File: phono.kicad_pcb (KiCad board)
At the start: 2 copper layers, 98.5 x 82 mm, 63 parts, among them J1 Power +30V, J2 R Phono in, J3 L Phono in, J4 R Phono out, J5 L Phono out, Q1 2N2222, Q2 2N2222, Q3 2N2222, Q4 2N2222, Q5 2N2222, Q6 2N2222

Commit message: Add files via upload
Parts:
- removed C10: 47uf, Capacitor_THT:CP_Radial_D6.3mm_P2.50mm
- removed C11, C12, C13, C14, C15, C16, C17: 150uf, Capacitor_THT:CP_Radial_D10.0mm_P5.00mm
- removed C18: 15uf, Capacitor_THT:CP_Radial_D5.0mm_P2.00mm
- removed C19, C21: 6.8nf, Capacitor_THT:C_Rect_L7.0mm_W2.0mm_P5.00mm
- removed C20, C22: 22nf, Capacitor_THT:C_Rect_L7.0mm_W2.0mm_P5.00mm
- removed D1, D2: 1N5250B, Diode_THT:D_DO-41_SOD81_P10.16mm_Horizontal
- removed J4: R Phono out, Connector_Wire:SolderWire-2sqmm_1x01_D2mm_OD3.9mm
- removed J5: L Phono out, Connector_Wire:SolderWire-2sqmm_1x01_D2mm_OD3.9mm
- removed Q4, Q5, Q6: 2N2222, Package_TO_SOT_THT:TO-18-3
- removed R16: 47k, Resistor_THT:R_Axial_DIN0207_L6.3mm_D2.5mm_P10.16mm_Horizontal
- removed R17: 8k2, Resistor_THT:R_Axial_DIN0207_L6.3mm_D2.5mm_P10.16mm_Horizontal
- removed R18: 150, Resistor_THT:R_Axial_DIN0207_L6.3mm_D2.5mm_P10.16mm_Horizontal
- removed R19, R26: 1k8, Resistor_THT:R_Axial_DIN0207_L6.3mm_D2.5mm_P10.16mm_Horizontal
- removed R20: 1k, Resistor_THT:R_Axial_DIN0207_L6.3mm_D2.5mm_P10.16mm_Horizontal
- removed R21: 12k, Resistor_THT:R_Axial_DIN0207_L6.3mm_D2.5mm_P10.16mm_Horizontal
- removed R22: 270k, Resistor_THT:R_Axial_DIN0207_L6.3mm_D2.5mm_P10.16mm_Horizontal
- removed R23: 680, Resistor_THT:R_Axial_DIN0207_L6.3mm_D2.5mm_P10.16mm_Horizontal
- removed R24: 6k, Resistor_THT:R_Axial_DIN0207_L6.3mm_D2.5mm_P10.16mm_Horizontal
- removed R25: 100, Resistor_THT:R_Axial_DIN0207_L6.3mm_D2.5mm_P10.16mm_Horizontal
- removed R27: 4k7, Resistor_THT:R_Axial_DIN0207_L6.3mm_D2.5mm_P10.16mm_Horizontal
- removed R28: 10k, Resistor_THT:R_Axial_DIN0207_L6.3mm_D2.5mm_P10.16mm_Horizontal
- added C101: 300u, Capacitor_THT:CP_Radial_D10.0mm_P5.00mm, F.Cu at (86.2, 96.3)
- added C102: 300u, Capacitor_THT:CP_Radial_D10.0mm_P5.00mm, F.Cu at (77.1, 85.1)
- added C103: 6n8, Capacitor_THT:C_Axial_L3.8mm_D2.6mm_P10.00mm_Horizontal, F.Cu at (96.3, 79.7)
- added C104: 22n, Capacitor_THT:C_Axial_L3.8mm_D2.6mm_P10.00mm_Horizontal, F.Cu at (103.9, 79.7)
- added C105: 47u, Capacitor_THT:CP_Radial_D10.0mm_P5.00mm, F.Cu at (121.0, 96.3)
- added C106: 1uF, Capacitor_THT:C_Axial_L3.8mm_D2.6mm_P10.00mm_Horizontal, F.Cu at (73.4, 69.8)
- added Down-Left1: MountingHole_3.2mm_M3, MountingHole:MountingHole_3.2mm_M3, F.Cu at (62.9, 109.9)
- added Down-Right1: MountingHole_3.2mm_M3, MountingHole:MountingHole_3.2mm_M3, F.Cu at (121.8, 109.9)
- added Q101: 2N2222, Package_TO_SOT_THT:TO-39-3, F.Cu at (88.6, 90.0)
- added Q102: 2N2222, Package_TO_SOT_THT:TO-39-3, F.Cu at (99.4, 90.0)
- added Q103: 2N2222, Package_TO_SOT_THT:TO-39-3, F.Cu at (110.2, 90.0)
- added R101: 150, Resistor_THT:R_Axial_DIN0207_L6.3mm_D2.5mm_P10.16mm_Horizontal, F.Cu at (75.4, 96.4)
- added R102: 1K8, Resistor_THT:R_Axial_DIN0207_L6.3mm_D2.5mm_P10.16mm_Horizontal, F.Cu at (79.2, 106.6)
- added R103: 8K2, Resistor_THT:R_Axial_DIN0207_L6.3mm_D2.5mm_P10.16mm_Horizontal, F.Cu at (88.6, 69.7)
- added R104: 100, Resistor_THT:R_Axial_DIN0207_L6.3mm_D2.5mm_P10.16mm_Horizontal, F.Cu at (77.5, 69.7)
- added R105: 12K, Resistor_THT:R_Axial_DIN0207_L6.3mm_D2.5mm_P10.16mm_Horizontal, F.Cu at (92.5, 79.9)
- added R106: 270K, Resistor_THT:R_Axial_DIN0207_L6.3mm_D2.5mm_P10.16mm_Horizontal, F.Cu at (100.1, 79.9)
- added R107: 6K, Resistor_THT:R_Axial_DIN0207_L6.3mm_D2.5mm_P10.16mm_Horizontal, F.Cu at (107.7, 79.9)
- added R108: 100, Resistor_THT:R_Axial_DIN0207_L6.3mm_D2.5mm_P10.16mm_Horizontal, F.Cu at (93.3, 95.1)
- added R109: 1K8, Resistor_THT:R_Axial_DIN0207_L6.3mm_D2.5mm_P10.16mm_Horizontal, F.Cu at (108.1, 95.1)
- added R110: 1K, Resistor_THT:R_Axial_DIN0207_L6.3mm_D2.5mm_P10.16mm_Horizontal, F.Cu at (71.6, 96.4)
- added R112: 47K, Resistor_THT:R_Axial_DIN0207_L6.3mm_D2.5mm_P10.16mm_Horizontal, F.Cu at (81.3, 79.9)
- added R113: 4K7, Resistor_THT:R_Axial_DIN0207_L6.3mm_D2.5mm_P10.16mm_Horizontal, F.Cu at (111.1, 95.1)
- added R114: 10K, Resistor_THT:R_Axial_DIN0207_L6.3mm_D2.5mm_P10.16mm_Horizontal, F.Cu at (114.2, 95.1)
- added U1: LM317_TO-220, Package_TO_SOT_THT:TO-220-3_Vertical, F.Cu at (74.9, 28.2)
- added Up-Left: MountingHole_3.2mm_M3, MountingHole:MountingHole_3.2mm_M3, F.Cu at (62.9, 25.3)
- added Up-Right: MountingHole_3.2mm_M3, MountingHole:MountingHole_3.2mm_M3, F.Cu at (121.9, 25.3)
- C1, C2, C8, C9: value 150uf -> 300u
- C3: value 1uf -> 6n8; footprint Capacitor_THT:CP_Radial_D4.0mm_P2.00mm -> Capacitor_THT:C_Axial_L3.8mm_D2.6mm_P10.00mm_Horizontal
- C4: value 150uf -> 22n; footprint Capacitor_THT:CP_Radial_D10.0mm_P5.00mm -> Capacitor_THT:C_Axial_L3.8mm_D2.6mm_P10.00mm_Horizontal
- C5: value 47uf -> 47u; footprint Capacitor_THT:CP_Radial_D6.3mm_P2.50mm -> Capacitor_THT:CP_Radial_D10.0mm_P5.00mm
- C6: value 15uf -> 1uF; footprint Capacitor_THT:CP_Radial_D5.0mm_P2.00mm -> Capacitor_THT:C_Axial_L3.8mm_D2.6mm_P10.00mm_Horizontal
- C7: value 1uf -> 47u; footprint Capacitor_THT:CP_Radial_D4.0mm_P2.00mm -> Capacitor_THT:CP_Radial_D10.0mm_P5.00mm
- J1: value Power +30V -> Conn_01x03_Pin; footprint Connector_Wire:SolderWire-2sqmm_1x02_P7.8mm_D2mm_OD3.9mm -> TerminalBlock:TerminalBlock_bornier-3_P5.08mm
- J2: value R Phono in -> Conn_01x02_Pin; footprint Connector_Wire:SolderWire-2sqmm_1x01_D2mm_OD3.9mm -> TerminalBlock:TerminalBlock_bornier-2_P5.08mm
- J3: value L Phono in -> Conn_01x03_Pin; footprint Connector_Wire:SolderWire-2sqmm_1x01_D2mm_OD3.9mm -> TerminalBlock:TerminalBlock_bornier-3_P5.08mm
- Q1, Q2, Q3: footprint Package_TO_SOT_THT:TO-18-3 -> Package_TO_SOT_THT:TO-39-3
- R1: value 100 -> 150
- R10: value 270k -> 1K
- R11: value 6k -> 1K
- R12: value 680 -> 47K
- R13: value 4k7 -> 4K7
- R14: value 10k -> 10K
- R15: value 100 -> 15K
- R2: value 47k -> 1K8
- R3: value 150 -> 8K2
- R4: value 1k8 -> 100
- R5: value 1k -> 12K
- R6: value 8k2 -> 270K
- R7: value 1k8 -> 6K
- R9: value 12k -> 1K8
- moved J1 136.2 mm to (65.7, 42.0), turned to -90 degrees
- moved R12 122.7 mm to (81.3, 41.3), turned to -90 degrees
- moved R11 118.2 mm to (86.2, 38.0)
- moved C6 113.1 mm to (73.7, 51.4), turned to 90 degrees
- moved J2 105.9 mm to (120.5, 32.0), turned to -90 degrees
- moved R10 104.9 mm to (72.8, 54.6), turned to -90 degrees
- moved Q3 97.9 mm to (110.5, 48.3), turned to 90 degrees
- moved Q2 97.4 mm to (99.7, 48.3)
- moved R13 96.6 mm to (110.7, 53.3), turned to -90 degrees
- moved R14 96.2 mm to (113.8, 53.3), turned to -90 degrees
- moved R6 95.5 mm to (104.4, 38.1), turned to 90 degrees
- moved R3 93.1 mm to (93.2, 27.8), turned to -90 degrees
- moved C3 89.4 mm to (100.3, 37.8), turned to 90 degrees
- moved R7 87.9 mm to (111.6, 27.9), turned to -90 degrees
- moved C4 87.3 mm to (108.1, 37.9)
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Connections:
- C2 pad 1: Net-(C14-Pad1) -> Net-(C2-Pad1)
- C3 pad 1: Net-(C3-Pad1) -> Net-(Q1-E)
- C3 pad 2: Net-(J2-Pin_1) -> Net-(C3-Pad2)
- C4 pad 1: Net-(C15-Pad1) -> Net-(C3-Pad2)
- C4 pad 2: GND -> Net-(Q2-C)
- C5 pad 1: Net-(D1-K) -> Net-(Q3-E)
- C5 pad 2: GND -> Output-R
- C6 pad 1: Net-(Q3-E) -> Input-R
- C6 pad 2: Net-(J4-Pin_1) -> Net-(C6-Pad2)
- C7 pad 1: Net-(C7-Pad1) -> +20V
- C7 pad 2: Net-(J3-Pin_1) -> GND
- C9 pad 1: Net-(C8-Pad1) -> Net-(C9-Pad1)
- J1 pad 1: +28V -> Input-R
- J2 pad 1: Net-(J2-Pin_1) -> +28V
- J3 pad 1: Net-(J3-Pin_1) -> Output-R
- R1 pad 1: Net-(Q1-B) -> Net-(Q1-E)
- R1 pad 2: Net-(C3-Pad1) -> Net-(C1-Pad1)
- R10 pad 1: Net-(Q2-C) -> Net-(C2-Pad1)
- R10 pad 2: Net-(C19-Pad1) -> Net-(C8-Pad1)
- R11 pad 1: +28V -> +20V
- R11 pad 2: Net-(Q2-C) -> Net-(U1-ADJ)
- R12 pad 1: +28V -> Net-(Q1-B)
- R12 pad 2: Net-(D1-K) -> Net-(C2-Pad1)
- R14 pad 1: Net-(J4-Pin_1) -> Output-R
- R15 pad 1: Net-(Q4-B) -> Net-(U1-ADJ)
- R15 pad 2: Net-(C7-Pad1) -> GND
- R2 pad 2: Net-(Q1-B) -> GND
- R3 pad 1: Net-(Q1-E) -> +20V
- R3 pad 2: Net-(C14-Pad1) -> Net-(Q1-C)
- R4 pad 1: Net-(C14-Pad1) -> Net-(C6-Pad2)
- R4 pad 2: GND -> Net-(Q1-B)
- R5 pad 1: Net-(C15-Pad1) -> Net-(Q1-E)
- R5 pad 2: Net-(C1-Pad1) -> Net-(C3-Pad2)
- R6 pad 1: Net-(D1-K) -> Net-(C3-Pad2)
- R6 pad 2: Net-(Q1-C) -> Net-(Q2-C)
- R7 pad 1: Net-(C15-Pad1) -> Net-(Q2-C)
- R7 pad 2: GND -> +28V
- R8 pad 2: Net-(C15-Pad1) -> Net-(C8-Pad1)
- R9 pad 1: Net-(C19-Pad1) -> Net-(C8-Pad1)
- R9 pad 2: Net-(Q1-E) -> GND
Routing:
- net +20V: track 0.00 -> 96.2 mm
- net Net-(C16-Pad1): track 75.8 -> 0.00 mm
- net Net-(Q4-E): track 63.5 -> 0.00 mm
- net Net-(C15-Pad1): track 61.0 -> 0.00 mm
- net Output-L: track 0.00 -> 47.7 mm
- net Net-(C11-Pad1): track 45.8 -> 0.00 mm
- net Net-(C9-Pad1): track 0.00 -> 42.2 mm
- net Net-(Q102-C): track 0.00 -> 41.2 mm
- net Net-(C14-Pad1): track 37.7 -> 0.00 mm
- net GND: track 316.9 -> 354.3 mm
- net Net-(Q4-C): track 37.0 -> 0.00 mm
- net Net-(Q101-E): track 0.00 -> 36.3 mm
- net Net-(C102-Pad1): track 0.00 -> 34.3 mm
- net Net-(Q4-B): track 32.6 -> 0.00 mm
- net Net-(Q5-C): track 28.0 -> 0.00 mm
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- added copper zone on B.Cu, net GND
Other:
- board size 98.5 x 82 mm -> 68.8 x 94.5 mm
- board text added: "GND +30V"
- board text added: "In_L GND In_R"
- board text added: "MM Phone Preamplifier RIAA (3x2N222A)"
- board text added: "Out_L GND Out_R"
- board text added: "Pedro Martin 2023-10-27"

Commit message: Add files via upload
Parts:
- added C10: 10u, Capacitor_THT:CP_Radial_D5.0mm_P2.00mm, F.Cu at (77.5, 34.8)
- R11: value 1K -> 220
- R15: value 15K -> 4K7
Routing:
- net Net-(U1-ADJ): track 18.8 -> 22.4 mm
- net GND: track 354.3 -> 357.4 mm

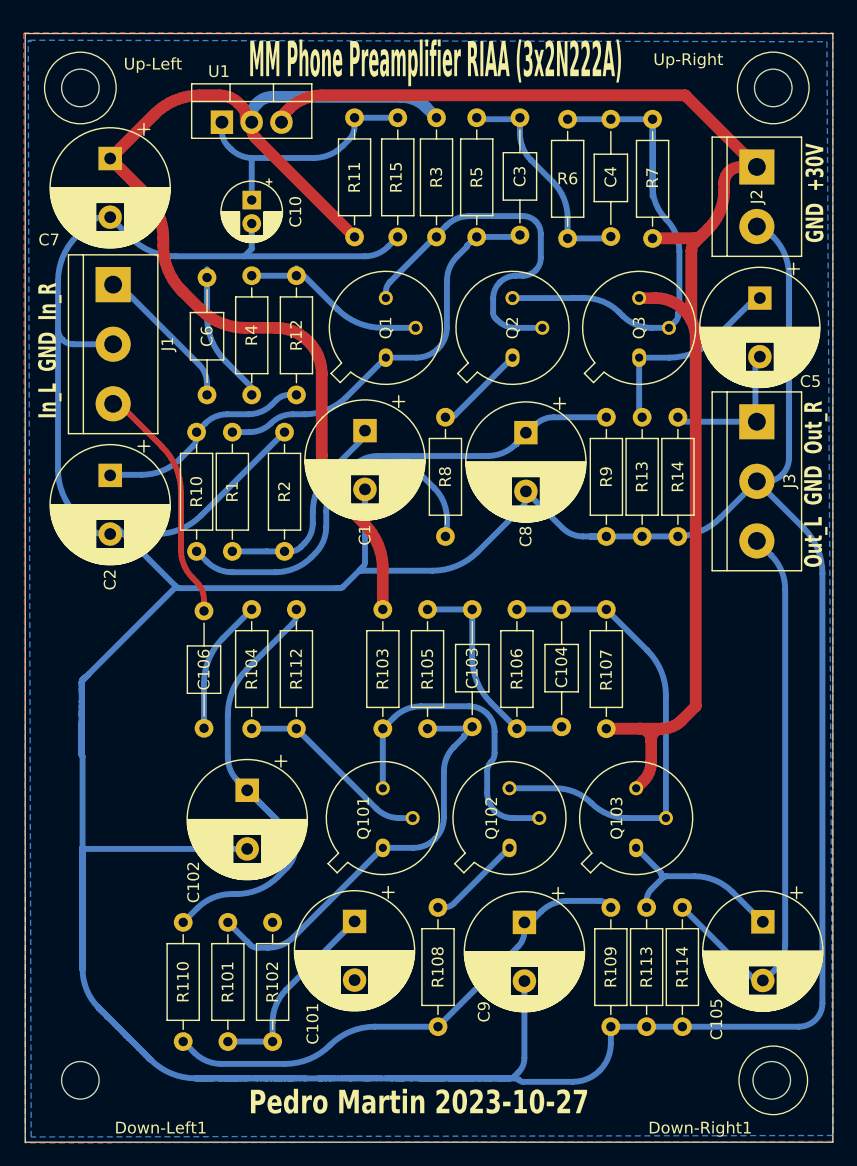
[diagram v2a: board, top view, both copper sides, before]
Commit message: Add files via upload
Esquema y placa actualizados para uso con Kicad 8
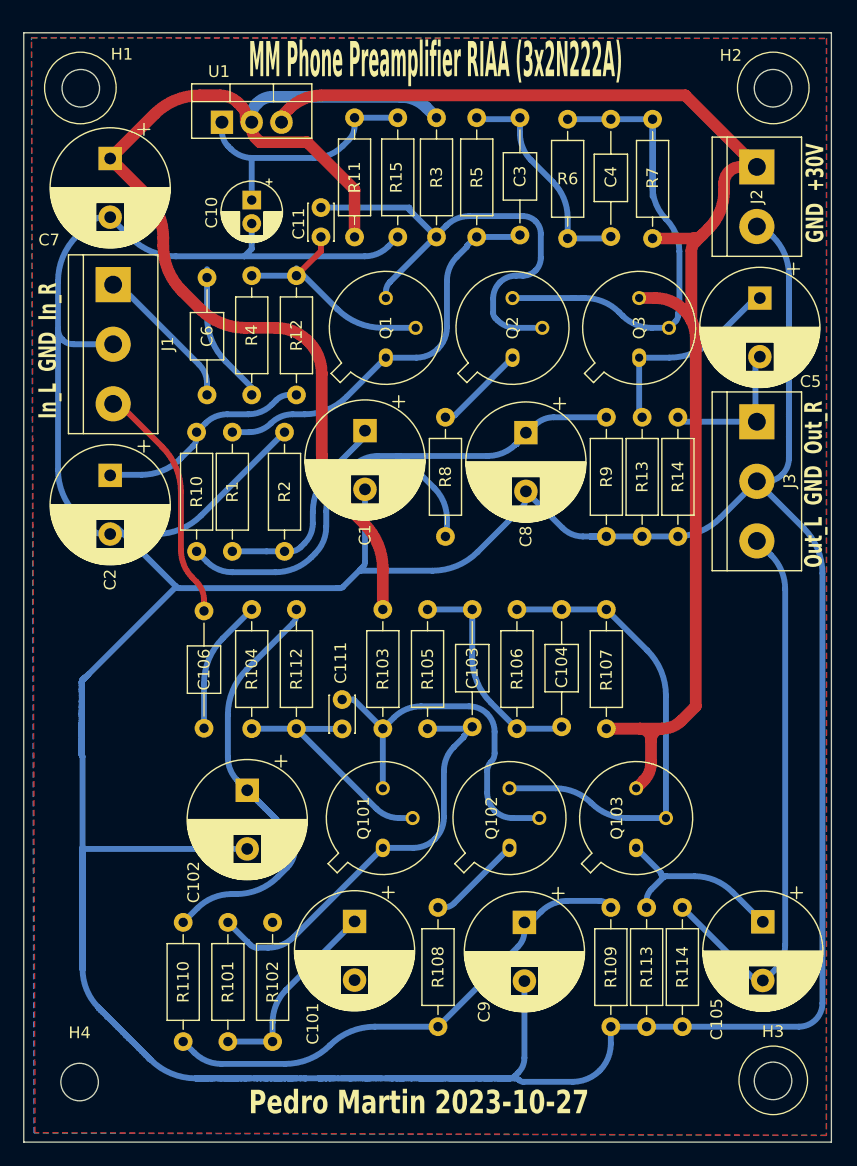
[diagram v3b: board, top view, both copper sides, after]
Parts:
- removed Down-Left1, Down-Right1, Up-Left, Up-Right: MountingHole_3.2mm_M3, MountingHole:MountingHole_3.2mm_M3
- added C11: 3p3, Capacitor_THT:C_Disc_D3.0mm_W2.0mm_P2.50mm, F.Cu at (83.4, 35.5)
- added C111: 3p3, Capacitor_THT:C_Disc_D3.0mm_W2.0mm_P2.50mm, F.Cu at (85.2, 77.4)
- added H1: MountingHole, MountingHole:MountingHole_3.2mm_M3, F.Cu at (62.9, 25.3)
- added H2: MountingHole, MountingHole:MountingHole_3.2mm_M3, F.Cu at (121.9, 25.3)
- added H3: MountingHole, MountingHole:MountingHole_3.2mm_M3, F.Cu at (121.9, 109.9)
- added H4: MountingHole, MountingHole:MountingHole_3.2mm_M3, F.Cu at (62.8, 110.0)
- R15: value 4K7 -> 3K3
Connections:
- net +28V renamed +VCC
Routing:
- net Net-(Q1-C): track 31.4 -> 42.4 mm
- net Net-(Q101-C): track 27.5 -> 32.0 mm
- net Net-(Q1-B): track 15.8 -> 20.0 mm
- net Net-(Q101-B): track 16.7 -> 20.6 mm
- net +20V: track 96.2 -> 98.5 mm
